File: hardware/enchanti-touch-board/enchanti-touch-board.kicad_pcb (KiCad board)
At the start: 2 copper layers, 72.4 x 31.8 mm, 92 parts, among them J2 Progamming Header, U1 CY8C4149AZI-S598

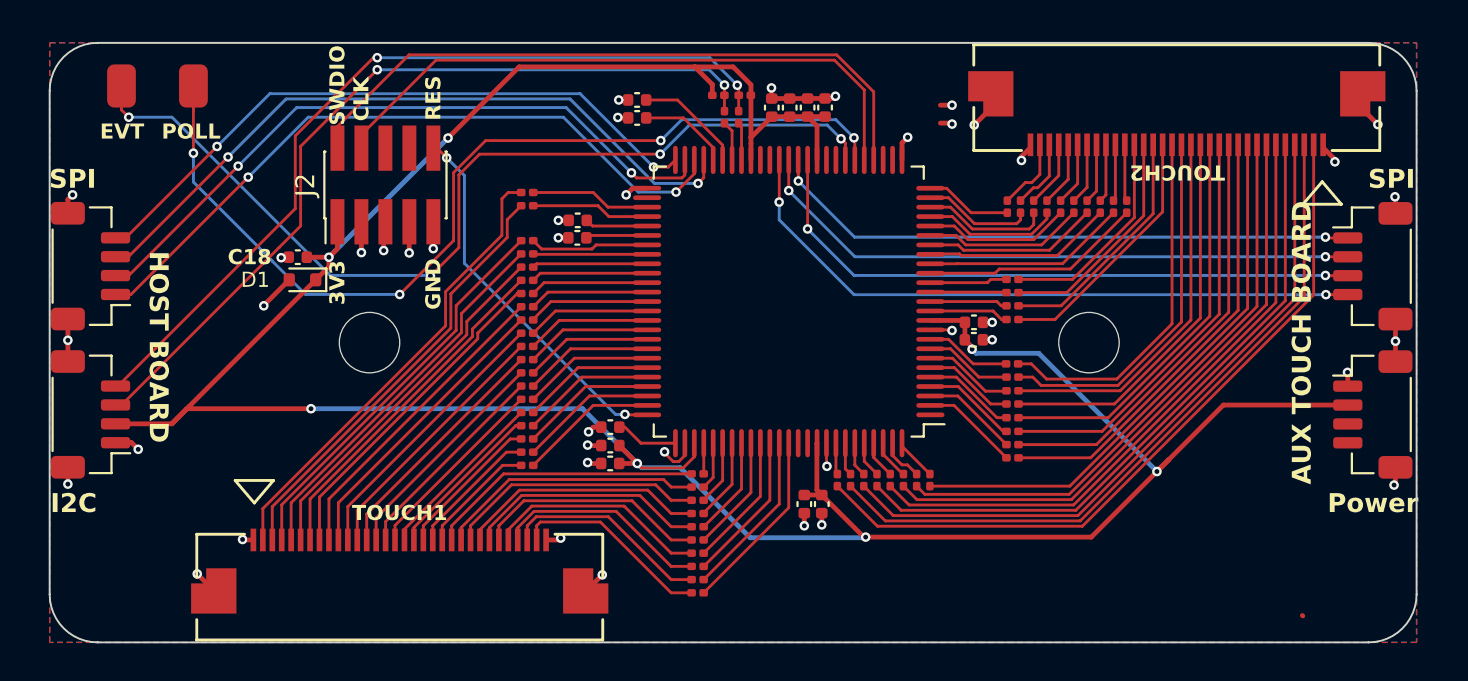
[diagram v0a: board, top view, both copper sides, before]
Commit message: Updated manufacturing files for board-rev3, added CANFD connector from board, removed redundant I2C connector
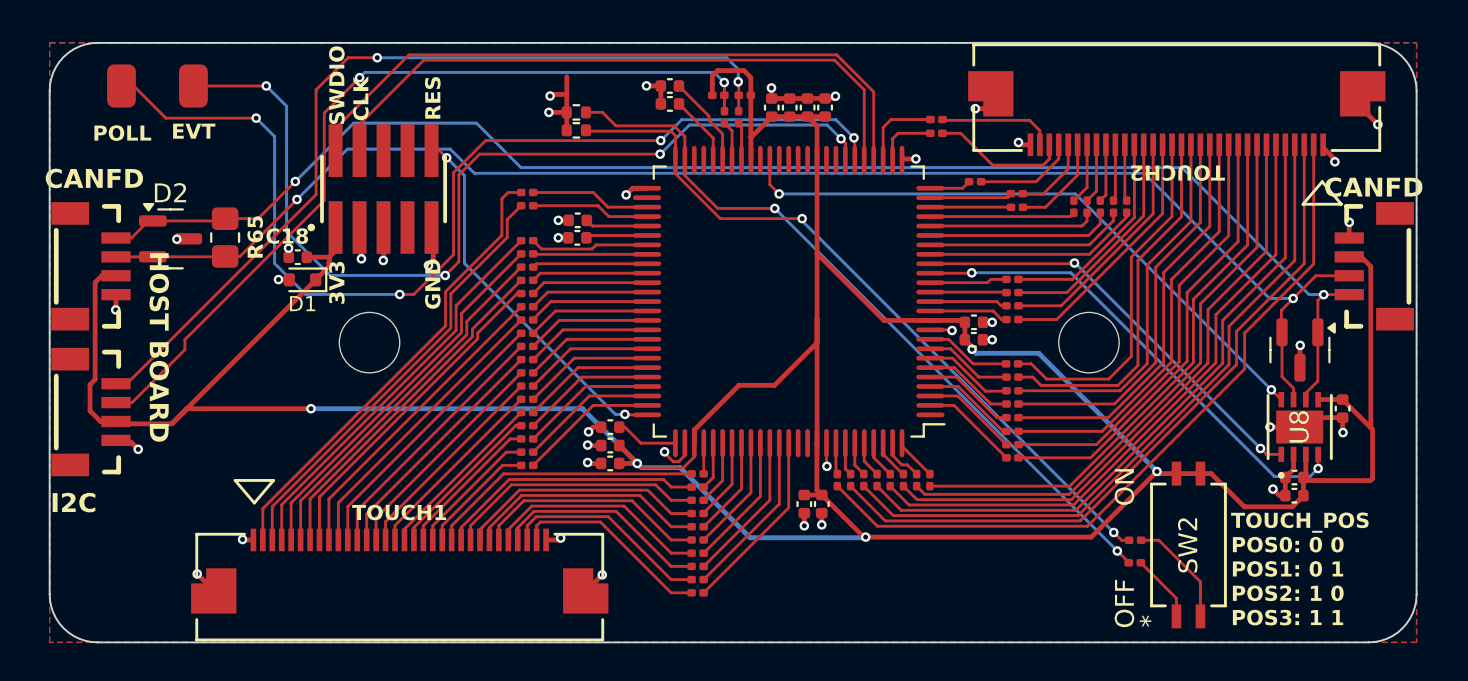
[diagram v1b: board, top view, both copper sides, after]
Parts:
- removed GPIO1, GPIO2: I2C, JST-footprints:JST_SH_BM04B-SRSS-TB_1x04-1MP_P1.00mm_Vertical
- removed GPIO3: SPI1, JST-footprints:JST_SH_BM04B-SRSS-TB_1x04-1MP_P1.00mm_Vertical
- removed GPIO4: SPI2, JST-footprints:JST_SH_BM04B-SRSS-TB_1x04-1MP_P1.00mm_Vertical
- removed J2: Progamming Header, Connector_PinHeader_1.27mm:PinHeader_2x05_P1.27mm_Vertical_SMD
- added C59: 1uF, Capacitor_SMD:C_0402_1005Metric, F.Cu at (209.4, 73.8)
- added C61: 0.1uF, Capacitor_SMD:C_0402_1005Metric, F.Cu at (212.0, 70.2)
- added C66: 0.1uF, Capacitor_SMD:C_0402_1005Metric, F.Cu at (209.4, 74.8)
- added CANFD1: JST-SH-1x04 1.0mm, ENCHANTI_connectors:JST_SMD_1.0mm-4_Vertical, F.Cu at (213.8, 62.6)
- added CANFD2: JST-SH-1x04 1.0mm, ENCHANTI_connectors:JST_SMD_1.0mm-4_Vertical, F.Cu at (145.5, 62.6)
- added D2: NUP2105L, Package_TO_SOT_SMD:SOT-23, F.Cu at (149.9, 61.2)
- added D3: NUP2105L, Package_TO_SOT_SMD:SOT-23, F.Cu at (209.7, 67.1)
- added I2C1: JST-SH-1x04 1.0mm, ENCHANTI_connectors:JST_SMD_1.0mm-4_Vertical, F.Cu at (145.5, 70.4)
- added J1: Programming Header, ENCHANTI_connectors:SAMTEC_FTSH-105-01-F-DV-P-TR, F.Cu at (161.2, 58.5)
- added R65: 120, Resistor_SMD:R_0805_2012Metric_Pad1.20x1.40mm_HandSolder, F.Cu at (152.8, 61.1)
- added R66: 330, Resistor_SMD:R_0201_0603Metric, F.Cu at (201.0, 78.3)
- added R67: 330, Resistor_SMD:R_0201_0603Metric, F.Cu at (201.0, 77.1)
- added R71: 10k, Resistor_SMD:R_0402_1005Metric, F.Cu at (171.4, 55.4)
- added R72: 10k, Resistor_SMD:R_0402_1005Metric, F.Cu at (171.4, 54.5)
- added SW2: SW_DIP_x02, ENCHANTI_switches:TDA02H0SB1R_CNK, F.Cu at (203.8, 77.4)
- added U8: TCAN3413DRBR, ENCHANTI_transceivers:VSON8-DRB_TEX, F.Cu at (209.7, 71.1)
- moved R32 5.95 mm to (190.5, 54.9), turned to 0 degrees
- moved R31 5.91 mm to (190.5, 55.6), turned to 0 degrees
- moved R30 3.37 mm to (192.5, 58.2), turned to 0 degrees
- moved R28 2.31 mm to (194.7, 59.5), turned to 0 degrees
- moved C7 1.89 mm to (176.4, 54.0)
- moved C6 1.89 mm to (176.4, 53.1)
- moved R29 1.74 mm to (194.7, 58.8), turned to 0 degrees
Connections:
- GPIO5 pad 1: /POLL_MAIN -> /EVT_MAIN
- GPIO5 pad 2: /EVT_MAIN -> /POLL_MAIN
- R23 pad 1: /MSC020 -> /MSC022
- R24 pad 1: /MSC021 -> /MSC023
- R25 pad 1: /MSC022 -> /MSC024
- R26 pad 1: /MSC023 -> /MSC025
- R27 pad 1: /MSC024 -> /MSC026
- R28 pad 1: /MSC025 -> /MSC027
- R29 pad 1: /MSC026 -> /MSC028
- R30 pad 1: /MSC027 -> /MSC029
- R31 pad 1: /MSC028 -> /MSC030
- R32 pad 1: /MSC029 -> /MSC031
- U1 pad 16: /MSC020 -> /FDCAN1_RX
- U1 pad 17: /MSC021 -> /FDCAN1_TX
- U1 pad 27: unconnected-(U1-P3.0-Pad27) -> /MSC030
- U1 pad 28: unconnected-(U1-P3.1-Pad28) -> /MSC031
- U1 pad 36: /COPI_AUX -> unconnected-(U1-P11.0-Pad36)
- U1 pad 37: /CIPO_AUX -> unconnected-(U1-P11.1-Pad37)
- U1 pad 38: /SCLK_AUX -> unconnected-(U1-P11.2-Pad38)
- U1 pad 39: /CS_AUX -> unconnected-(U1-P11.3-Pad39)
- U1 pad 40: /SPIMODE -> /CAN_MODE
- U1 pad 47: /COPI_MAIN -> unconnected-(U1-P4.4-Pad47)
- U1 pad 48: /CIPO_MAIN -> unconnected-(U1-P4.5-Pad48)
- U1 pad 49: /SCLK_MAIN -> /POS_P1
- U1 pad 50: /CS_MAIN -> /POS_P2
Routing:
- net /CAN_L: track 0.00 -> 77.6 mm, vias 0 -> 2
- net /CAN_H: track 0.00 -> 77.3 mm, vias 0 -> 2
- net /POS_P1: track 0.00 -> 39.8 mm, vias 0 -> 2
- net /POS_P2: track 0.00 -> 39.0 mm, vias 0 -> 2
- net /COPI_MAIN: track 37.5 -> 0.00 mm, vias 2 -> 0
- net /CIPO_MAIN: track 37.3 -> 0.00 mm, vias 2 -> 0
- net /SCLK_MAIN: track 36.2 -> 0.00 mm, vias 2 -> 0
- net +3V3: track 156.4 -> 192.5 mm, vias 7 -> 5
- net /CS_AUX: track 34.9 -> 0.00 mm, vias 2 -> 0
- net /CS_MAIN: track 34.6 -> 0.00 mm, vias 2 -> 0
- net /COPI_AUX: track 33.3 -> 0.00 mm, vias 2 -> 0
- net /CAN_MODE: track 0.00 -> 33.1 mm, vias 0 -> 2
- net /SCLK_AUX: track 32.7 -> 0.00 mm, vias 2 -> 0
- net /CIPO_AUX: track 31.5 -> 0.00 mm, vias 2 -> 0
- net /FDCAN1_RX: track 0.00 -> 25.9 mm, vias 0 -> 2
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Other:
- board text added: "CANFD"
- board text added: "Enchanti Touch Board v0.3 IDMIL, McGill University Albert Niyonsenga 2025/03"
- board text added: "TOUCH_POS POS0: 0 0 POS1: 0 1 POS2: 1 0 POS3: 1 1"
- board text removed: "AUX TOUCH BOARD"
- board text removed: "Enchanti Touch Board v0.2 IDMIL, McGill University Albert Niyonsenga 2023/12"
- board text removed: "Power"
- board text removed: "SPI"
